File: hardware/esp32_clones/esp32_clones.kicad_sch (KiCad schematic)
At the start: 20 parts, among them J2 USB_A, J3 USB_A, J4 USB_A, J5 Micro_SD_Card, J6 Barrel_Jack, J7 DA15_Pins, SW1 SW_Push

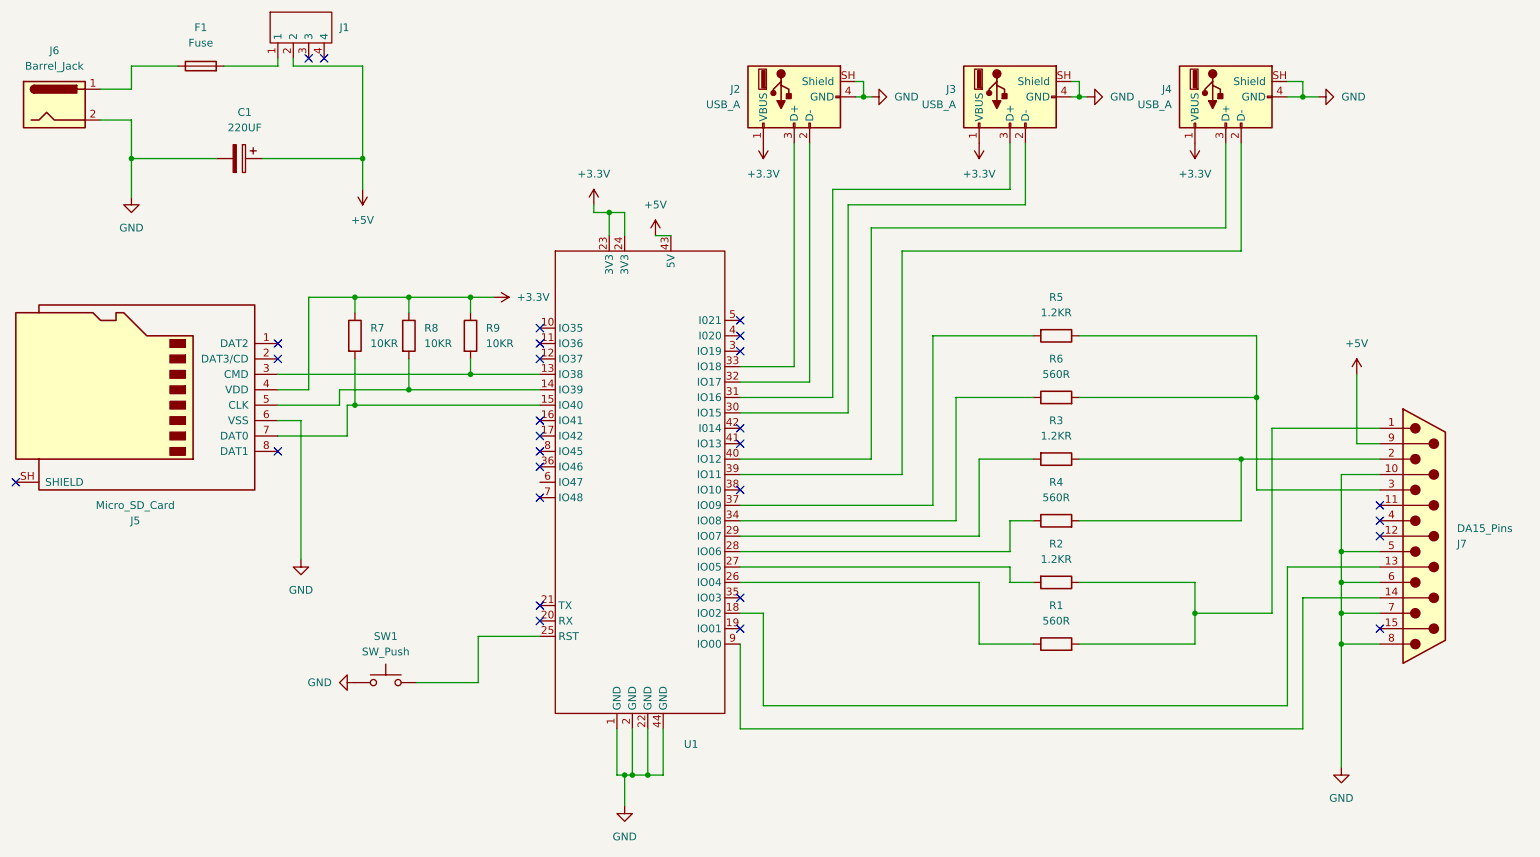
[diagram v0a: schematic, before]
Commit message: Add production files for ESP32 clone hardware
- Created BOM (bill of materials) file to list components and their specifications.
- Added designators file to map component designators to their respective quantities.
- Introduced IPC netlist file for electrical connections and layout.
- Included positions file to specify component placements on the PCB.
- Established symbol library table for component symbols used in the design.
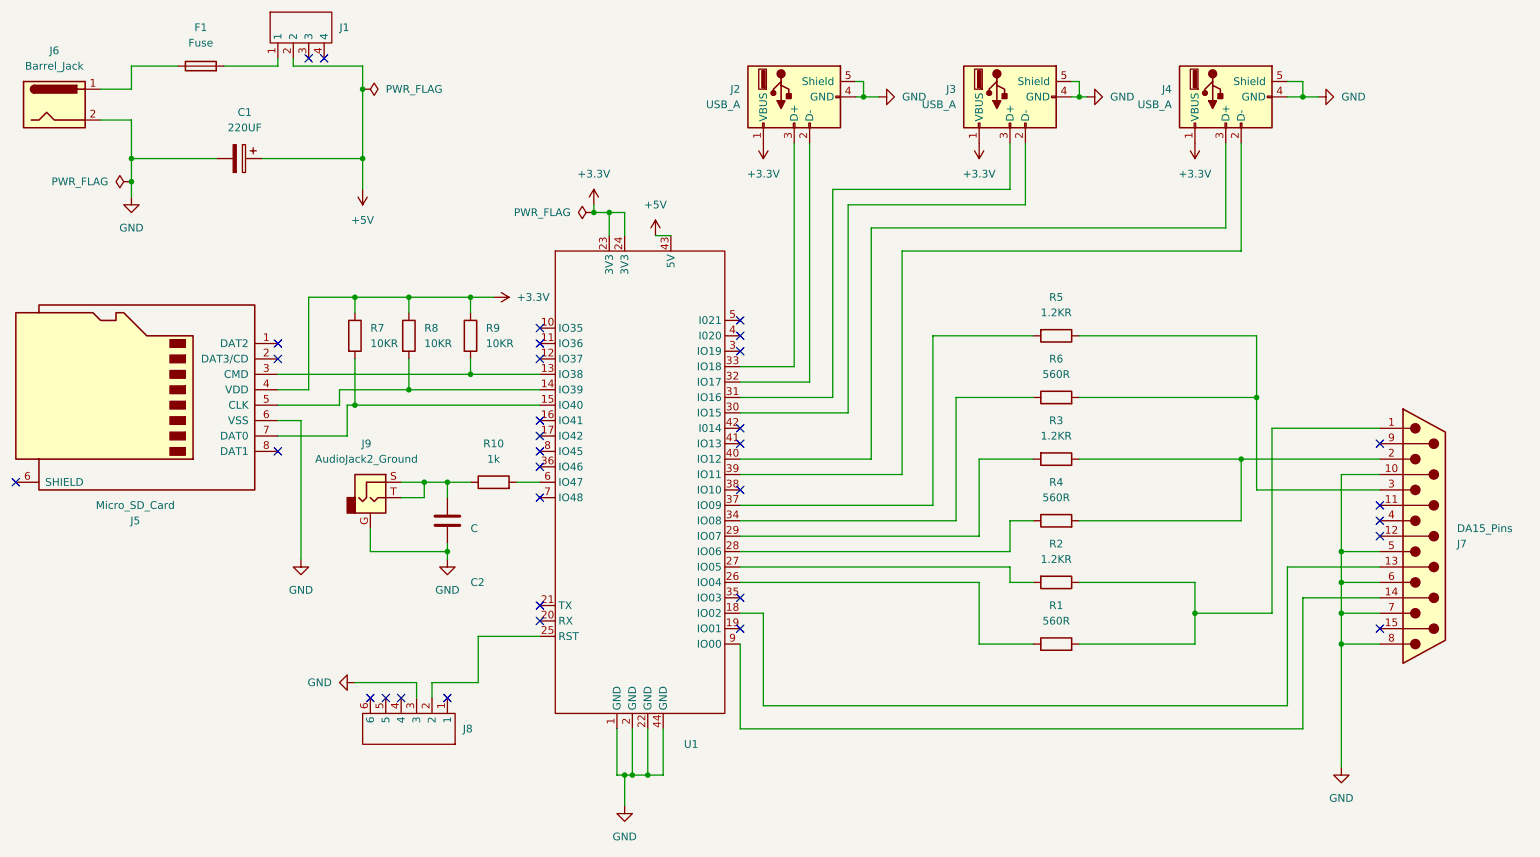
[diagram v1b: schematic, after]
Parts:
- removed SW1: SW_Push, symbol Switch:SW_Push
- added C2: C, Capacitor_SMD:C_0805_2012Metric_Pad1.18x1.45mm_HandSolder, symbol Device:C
- added J8: (no value), PS-22F05:PS-22F05, symbol ps-22f05:PS-22f05_1
- added J9: AudioJack2_Ground, PJ307:PJ-307, symbol Connector_Audio:AudioJack2_Ground
- added R10: 1k, Resistor_SMD:R_0805_2012Metric_Pad1.20x1.40mm_HandSolder, symbol Device:R
- J1: footprint libraries:PS-12E05 -> COCO2:PS-12E05
- J2, J3, J4: footprint libraries:TE_6364372-2 -> COCO2:TE_6364372-2
- J5: footprint libraries:Conn_uSDcard -> COCO2:Conn_uSDcard
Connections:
- net +5V: no longer J7.9 (P9)
- net GND: now also J2.5 (Shield), J3.5 (Shield), J4.5 (Shield), C2.2, J8.3, J9.G; no longer J2.SH (Shield), J3.SH (Shield), J4.SH (Shield)
- net at U1.25 (RST): now also J8.2
- net at U1.6 (IO47): now also R10.2
- new net: C2.1, J9.S, J9.T, R10.1
- no-connect marks 28 -> 33
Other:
- company: (none) -> The Retro Hacker
- title: (none) -> ESP32 Clones

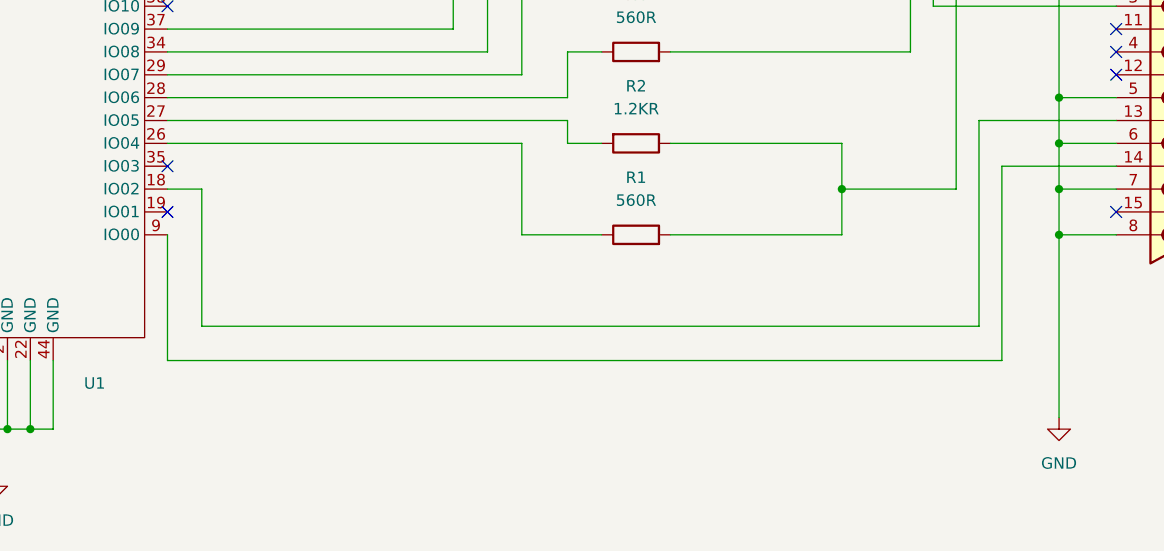
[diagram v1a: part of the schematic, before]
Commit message: ## 1.11 - 2026-08-19
### Added

- Added a progress gauge that runs while a firmware update is validated and copied.

### Changed

- Moved the USB keyboard port to GPIO11 and GPIO12, joystick 1 to GPIO15 and GPIO16, and joystick 2 to GPIO17 and GPIO18, to simplify cable routing on the board.
- Gave every F12 screen the same layout, with the product name and screen title in the header, matching separator lines, and key hints in the footer. The disk image picker, firmware update screens, and error messages previously used their own styles.
- Renamed the "Joystick calibration" menu entry to "Joystick setup".
- Turned the joystick Serial debug output off by default.
- Listed only files with a matching extension when choosing a firmware or disk image, hiding folders such as System Volume Information that could not be opened anyway.
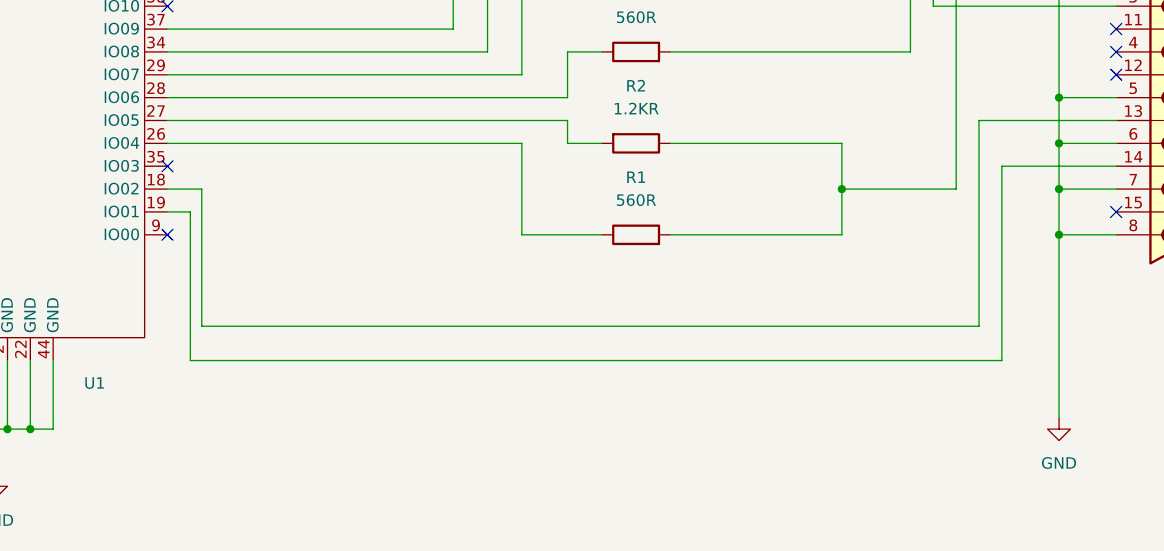
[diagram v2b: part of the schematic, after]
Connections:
- net at U1.19 (IO01): now also J7.14 (P14)
- net at U1.9 (IO00): no longer J7.14 (P14)
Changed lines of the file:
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@@
 	(title_block
 		(title "ESP32 Clones")
-		(date "2026-08-02")
-		(rev "1.0")
+		(date "2026-08-19")
+		(rev "1.1")
 		(company "The Retro Hacker")
 		(comment 2 "Commercial-ShareAlike 4.0 Internacional License")
@@
 	)
 	(no_connect
+		(at 152.4 119.38)
+	)
+	(no_connect
 		(at 119.38 82.55)
 	)
@@
 		(at 96.52 128.27)
 	)
-	(no_connect
-		(at 152.4 116.84)
-	)
 	(wire
 		(pts
@@
 	(wire
 		(pts
+			(xy 154.94 116.84) (xy 154.94 133.35)
+		)
+		(stroke
+			(width 0)
+			(type default)
+		)
+	)
+	(wire
+		(pts
 			(xy 99.06 128.27) (xy 99.06 125.73)
 		)
@@
 	(wire
 		(pts
-			(xy 152.4 133.35) (xy 245.11 133.35)
+			(xy 152.4 116.84) (xy 154.94 116.84)
 		)
 		(stroke
@@
 	(wire
 		(pts
-			(xy 152.4 133.35) (xy 152.4 119.38)
-		)
-		(stroke
-			(width 0)
-			(type default)
-		)
-	)
-	(wire
-		(pts
 			(xy 156.21 129.54) (xy 156.21 114.3)
 		)
@@
 		)
 		(stroke
+			(width 0)
+			(type default)
+		)
+	)
+	(wire
+		(pts
+			(xy 154.94 133.35) (xy 245.11 133.35)
+		)
+		(stroke

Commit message: Refactor code structure for improved readability and maintainability
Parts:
- J2: value USB_A -> Joystick 2
- J3: value USB_A -> Joystick 1
- J4: value USB_A -> Keyboard
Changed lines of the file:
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@@
 			)
 		)
-		(property "Value" "USB_A"
+		(property "Value" "Keyboard"
 			(at 223.52 30.4799 90)
 			(show_name no)
@@
 			)
 		)
-		(property "Value" "USB_A"
+		(property "Value" "Joystick 1"
 			(at 187.96 30.4799 90)
 			(show_name no)
@@
 			)
 		)
-		(property "Value" "USB_A"
+		(property "Value" "Joystick 2"
 			(at 152.4 30.4799 90)
 			(show_name no)

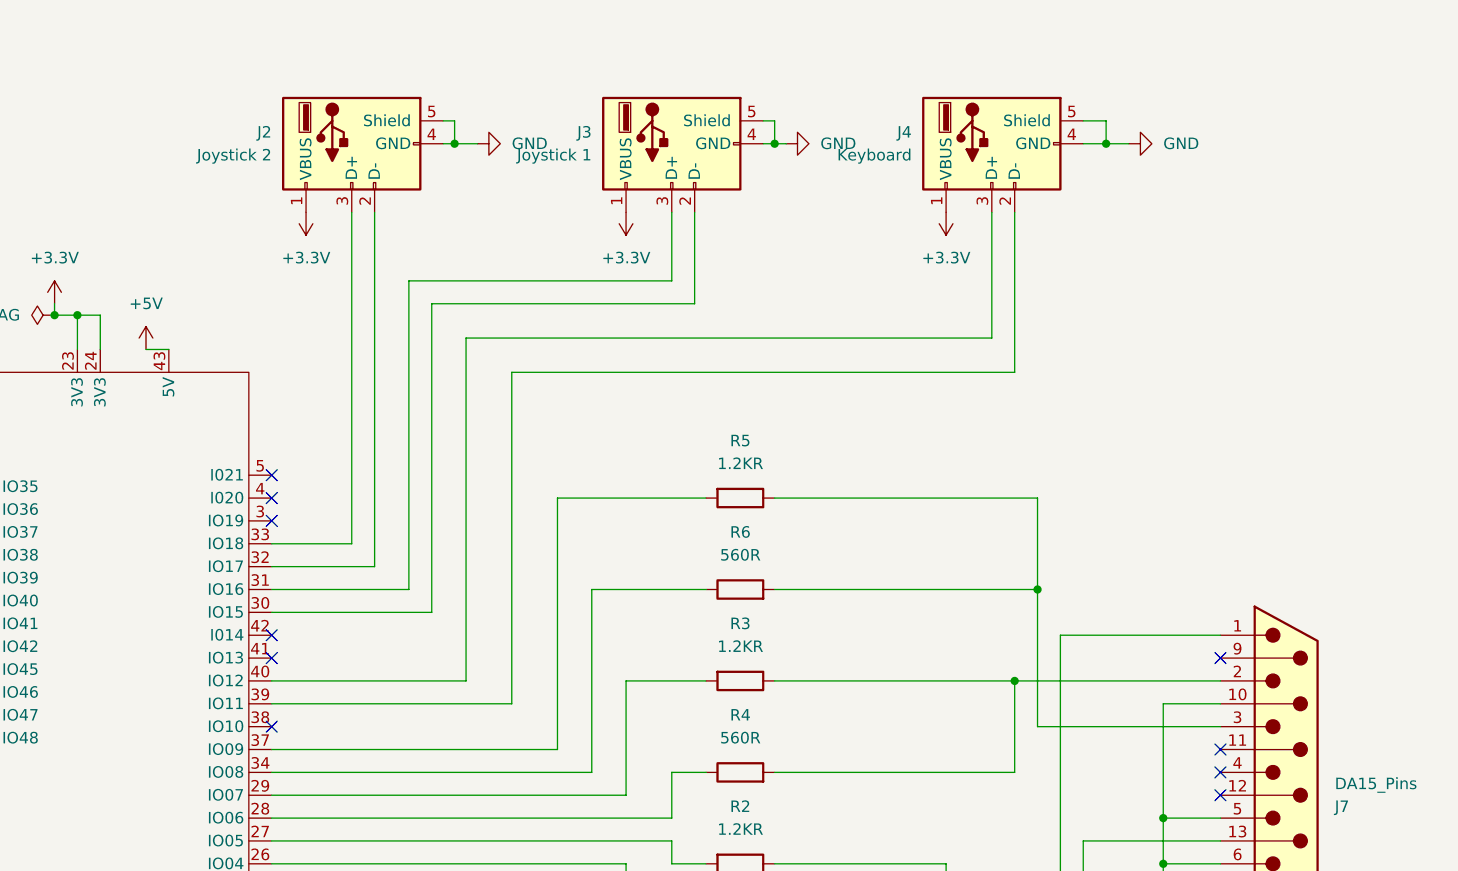
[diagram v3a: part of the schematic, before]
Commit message: Add USB-OTG host support for CP400 keyboard
- Implemented CP400UsbKeyboard.cpp to manage USB keyboard connections using the ESP32-S3 USB-OTG controller.
- Created CP400UsbKeyboard.h header file to declare functions for starting the USB keyboard and checking connection status.
- The new implementation allows for full-speed keyboard enumeration and improves compatibility with various USB keyboards.
- Hardware revision 1.2
- Moved the keyboard port to the ESP32-S3 native USB-OTG host on GPIO19 and GPIO20, so ordinary full speed USB keyboards now work. The previous bit-banged stack could only talk to low speed devices, which is why most keyboards appeared dead or never lit their indicators.
- Requested the HID boot protocol from the keyboard, so keyboards that default to their own report layout still deliver the standard report the emulator expects.
- Turned the native USB serial console off, because the keyboard host and the console cannot share the one USB controller. Serial output and firmware uploads now use the UART port, which already carried the boot log.
- Kept joystick 1 and joystick 2 on the existing bit-banged stack, unchanged.
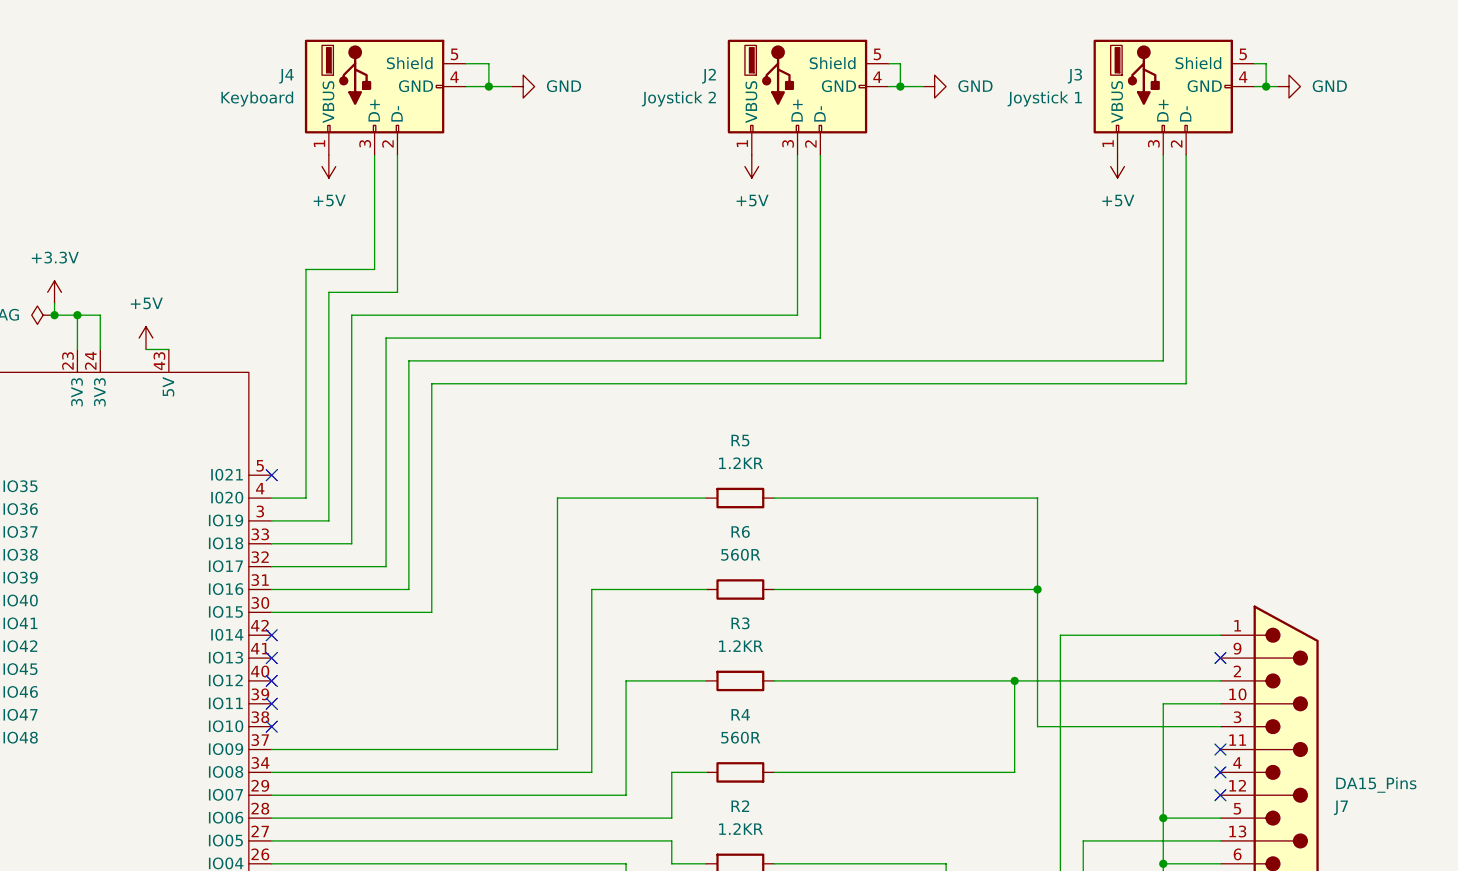
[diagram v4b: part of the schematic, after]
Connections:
- net +3.3V: no longer J2.1 (VBUS), J3.1 (VBUS), J4.1 (VBUS)
- net +5V: now also J2.1 (VBUS), J3.1 (VBUS), J4.1 (VBUS)
- net at U1.3 (IO19): now also J4.2 (D-)
- net at U1.39 (IO11): no longer J4.2 (D-)
- net at U1.4 (I020): now also J4.3 (D+)
- net at U1.40 (IO12): no longer J4.3 (D+)
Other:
- moved on the sheet: J2, J3, J4
